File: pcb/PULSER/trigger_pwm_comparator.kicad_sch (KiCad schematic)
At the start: 3 parts, among them U2 BD50FC0FP

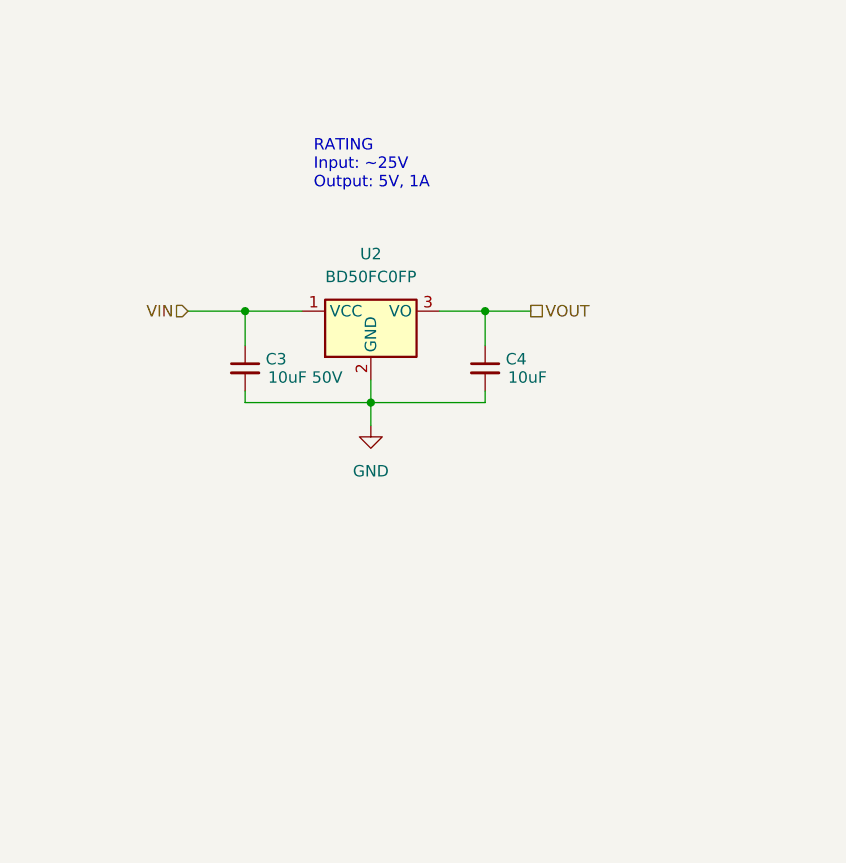
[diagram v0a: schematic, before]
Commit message: Rename pcb & firmware to be more meaningful
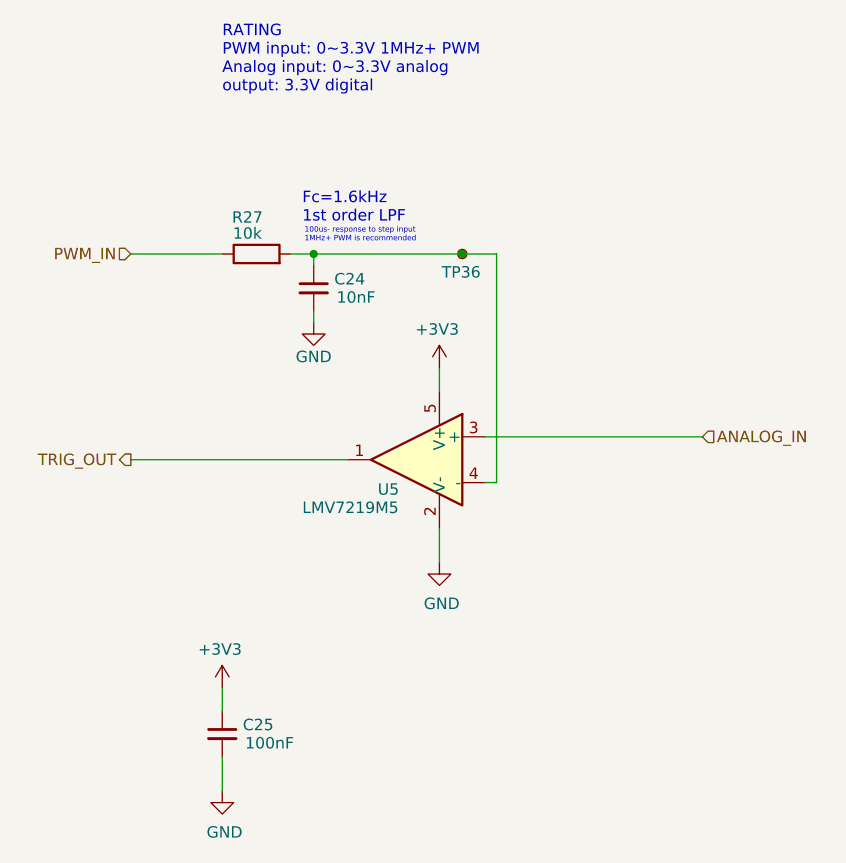
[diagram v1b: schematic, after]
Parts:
- removed C3: 10uF 50V, Capacitor_SMD:C_1206_3216Metric, symbol Device:C_Small
- removed C4: 10uF, Capacitor_SMD:C_0603_1608Metric, symbol Device:C_Small
- removed U2: BD50FC0FP, Package_TO_SOT_SMD:TO-252-2, symbol Regulator_Linear:BD50FC0FP
- added C24: 10nF, Capacitor_SMD:C_0603_1608Metric, symbol Device:C_Small
- added C25: 100nF, Capacitor_SMD:C_0603_1608Metric, symbol Device:C_Small
- added R27: 10k, Resistor_SMD:R_0603_1608Metric, symbol Device:R
- added TP36: TestPoint, TestPoint:TestPoint_Pad_D1.5mm, symbol Connector:TestPoint_Small
- added U5: LMV7219M5, Package_TO_SOT_SMD:SOT-23-5, symbol Comparator:LMV7219M5
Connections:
- net GND: now also C24.2, C25.2, U5.2 (V-)
- new net: C24.1, R27.2, TP36.1, U5.4 (-)
- new net +3V3: C25.1, U5.5 (V+)
- new net ANALOG_IN: U5.3 (+)
- new net PWM_IN: R27.1
- new net TRIG_OUT: U5.1
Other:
- note added: "100us- response to step input 1MHz+ PWM is recommended"
- note added: "Fc=1.6kHz 1st order LPF"
- note added: "RATING PWM input: 0~3.3V 1MHz+ PWM Analog input: 0~3.3V analog output: 3.3V digital"
- note removed: "RATING Input: ~25V Output: 5V, 1A"

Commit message: PULSER r2 pulse shaper draft
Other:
- title: CTRL-MINI-ED -> PULSER
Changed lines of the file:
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@@
 (kicad_sch
-	(version 20231120)
+	(version 20250114)
 	(generator "eeschema")
-	(generator_version "8.0")
+	(generator_version "9.0")
 	(paper "A4")
 	(title_block
-		(title "CTRL-MINI-ED")
-		(date "2024-12-11")
-		(rev "1")
+		(title "PULSER")
+		(date "2025-02-14")
+		(rev "2")
 		(company "Spark Project")
 		(comment 1 "Author: 夕月霞 (xyx)")
 		(comment 2 "EDM Pulse Generator Board")
+	)
+	(text "RATING\nPWM input: 0~3.3V 1MHz+ PWM\nAnalog input: 0~3.3V analog\noutput: 3.3V digital\n"
+		(exclude_from_sim no)
+		(at 71.12 26.67 0)
+		(effects
+			(font
+				(size 1.27 1.27)
+			)
+			(justify left)
+		)
+	)
+	(text "Fc=1.6kHz\n1st order LPF"
+		(exclude_from_sim no)
+		(at 80.01 43.18 0)
+		(effects
+			(font
+				(size 1.27 1.27)
+			)
+			(justify left)
+		)
+	)
+	(text "100us- response to step input\n1MHz+ PWM is recommended"
+		(exclude_from_sim no)
+		(at 80.264 46.228 0)
+		(effects
+			(font
+				(size 0.6 0.6)
+			)
+			(justify left)
+		)
 	)
 	(junction
@@
 			"4ZK0ekyCWdiZWsxzXcAo9v1YUwMLO1OLPV0XsB1b2ZmqWdiZqkjfmi5gpus6tjNTbillXRdhmoOF"
 			"namOFyRzFTVkDylMdSzsTHVSCb1lTF47jEkoCztTraSGSlLrMgljYWeqk9wVVFLrMgljYWeqNc91"
-			"AeOY57oA0xws7Ey1krqCSmpdJmEs7Ey1khoqSa3LJMz/BzS5D5EH5SGfAAAAAElFTkSuQmCC"
-		)
-	)
-	(text "RATING\nPWM input: 0~3.3V 1MHz+ PWM\nAnalog input: 0~3.3V analog\noutput: 3.3V digital\n"
-		(exclude_from_sim no)
-		(at 71.12 26.67 0)
+			"AeOY57oA0xws7Ey1krqCSmpdJmEs7Ey1khoqSa3LJMz/BzS5D5EH5SGfAAAAAElFTkSuQmCCT8IJ"
+			"CNhv/wKA0J/QvtC70YPQttC40YDQvdGL0LkAAAAA3AkO2AAAA4BOZ2hpw6puZwAAAAAAAAAAwGfl"
+			"RM8BAADeCQzYAAEDgEJvbGQgSXRhbGljAAACAoBDOi9XSU5ET9gJEthvAgOAAAAAAAAAAAA5Grt7"
+			"ZgAAAHDxzETPAQAA2gkQ2AADA4AGAAAAEAAAAPButv//////AAAAAAAAAADUCRbYAAQDgFNlZ29l"
+			"IFVJIEJsYWNrAIAAAAAAAAAAANYJFNgABQOAVmV0IEN1cnNpZWYAAAAAAAAAAAAAAAAA0Aka2M8G"
+			"A4AAAAAAAAAAADhA/mwAAAAA0PbMRM8BAADSCRjYAAcDgEt1cnNpdm9pdHUA2AAGAoDw+MxEzwEA"
+			"AOwJHtgACAOABgAAABAAAAAga7b//////wAAAAAAAAAA7gkc2AAJA4BQb2dydWJpb255AAAAAAAA"
+			"QPHMRM8BAADoCSLYAAoDgFBvxaFldm5vAAkj2AAIAoBQ88xEzwEAAOoJINgACwOA0J/QvtC70YPQ"
+			"ttC40YDQvdGL0LkAAAAA5Akm2AAMA4BTZWdvZSBVSQBTL2ZvbnRzXHZnYXN5c3LmCSTYAA0DgFNl"
+			"Z29lIFVJAAkl2M8KAoAAAAAAAAAAAOAJKtgADgOABgAAABAAAADwL7b//////wAAAAAAAAAA4gko"
+			"2AAPA4BTZWdvZSBVSQAAAAAAAAAAgKDoRM8BAAD8CS7YABADgNCa0YPRgNGB0LjQsgAMAoAAAAAA"
+			"AAAAAP4JLNgAEQOASXTDoWxpY28AAAAAAAAAAAAAAAAAAAAA+Aky2AASA4BTZWdvZSBVSSBTZW1p"
+			"bGlnaHQARM8BAAD6CTDYABMDgFR1xI1uw6kgS3VyesOtdmEA8sxEzwEAAPQJNtgAFAOAAAAAAAAA"
+			"AACnIqiqAAAAANDyzETPAQAA9gk02AAVA4BOZWdyaXRhIEN1cnNpdmEAQGflRM8BAADwCTrYABYD"
+			"gFNlbWlsaWdodAA72AAQAoAAAAAAAAAAAPIJONgAFwOARsOpbGvDtnbDqXIgRMWRbHQAAAAAAAAA"
+			"jAk+2AAYA4BUdcSNbsOhIEt1cnrDrXZhAGflRM8BAACOCTzYABkDgFNlZ29lIFVJAAk92M8SAoDQ"
+			"+sxEzwEAAIgJQtgAGgOAS2FsxLFuIMSwdGFsaWsAAAAAAAAAAAAAiglA2AAbA4BMaWhhdm9pdHUA"
+			"AAAAAAAA8GflRM8BAACECUbYABwDgE5lZ3JldGEgQ3Vyc2l2YQAA+MxEzwEAAIYJRNgAHQOAAAAA"
+			"AAAAAACIacCqAAAAAHD3zETPAQAAgAlK2AAeA4BTZWdvZSBVSSBMaWdodAAAUGflRM8BAA=="
+		)
+	)
+	(hierarchical_label "PWM_IN"
+		(shape input)
+		(at 60.96 48.26 180)
 		(effects
 			(font
 				(size 1.27 1.27)
 			)
-			(justify left)
-		)
-	)
-	(text "Fc=1.6kHz\n1st order LPF"
-		(exclude_from_sim no)
-		(at 80.01 43.18 0)
+			(justify right)
+		)
+	)
+	(hierarchical_label "TRIG_OUT"
+		(shape output)
+		(at 60.96 71.12 180)
 		(effects
 			(font
 				(size 1.27 1.27)
 			)
-			(justify left)
-		)
-	)
-	(text "100us- response to step input\n1MHz+ PWM is recommended"
-		(exclude_from_sim no)
-		(at 80.264 46.228 0)
-		(effects
-			(font
-				(size 0.6 0.6)
-			)
-			(justify left)
-		)
-	)
-	(hierarchical_label "PWM_IN"
-		(shape input)
-		(at 60.96 48.26 180)
-		(fields_autoplaced yes)
-		(effects
-			(font
-				(size 1.27 1.27)
-			)
-			(justify right)
-		)
-	)
-	(hierarchical_label "TRIG_OUT"
-		(shape output)
-		(at 60.96 71.12 180)
-		(fields_autoplaced yes)
-		(effects
-			(font
-				(size 1.27 1.27)
-			)
 			(justify right)
 		)
@@
 		(shape input)
 		(at 124.46 68.58 0)
-		(fields_autoplaced yes)
 		(effects
 			(font
@@
 		(at 81.28 55.88 0)
 		(unit 1)
-		(exclude_from_sim yes)
+		(exclude_from_sim no)
 		(in_bom yes)
 		(on_board yes)
@@
 		(at 71.12 107.95 0)
 		(unit 1)
-		(exclude_from_sim yes)
+		(exclude_from_sim no)
 		(in_bom yes)
 		(on_board yes)
@@
 		(at 95.25 82.55 0)
 		(unit 1)
-		(exclude_from_sim yes)
+		(exclude_from_sim no)
 		(in_bom yes)
 		(on_board yes)
